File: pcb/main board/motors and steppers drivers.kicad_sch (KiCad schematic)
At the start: 35 parts, among them J1 Motor 0 Conn, J2 Motor 1 Conn, J3 Motor 2 Conn, J4 Motor 3 Conn, J7 Stepper 0 Conn, J8 Stepper 1 Conn, J9 Stepper 2 Conn, U1 L298HN, U2 L298HN

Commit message: Modified LM2596S to be a module.
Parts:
- C1, C2, C3, C4: footprint (none) -> Capacitor_THT:C_Disc_D6.0mm_W2.5mm_P5.00mm
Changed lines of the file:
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@@
 			)
 		)
-		(property "Footprint" ""
+		(property "Footprint" "Capacitor_THT:C_Disc_D6.0mm_W2.5mm_P5.00mm"
 			(at 73.66 35.2552 0)
 			(effects
@@
 			)
 		)
-		(property "Footprint" ""
+		(property "Footprint" "Capacitor_THT:C_Disc_D6.0mm_W2.5mm_P5.00mm"
 			(at 55.88 35.2552 0)
 			(effects
@@
 			)
 		)
-		(property "Footprint" ""
+		(property "Footprint" "Capacitor_THT:C_Disc_D6.0mm_W2.5mm_P5.00mm"
 			(at 213.36 33.3248 0)
 			(effects
@@
 			)
 		)
-		(property "Footprint" ""
+		(property "Footprint" "Capacitor_THT:C_Disc_D6.0mm_W2.5mm_P5.00mm"
 			(at 195.58 33.3248 0)
 			(effects

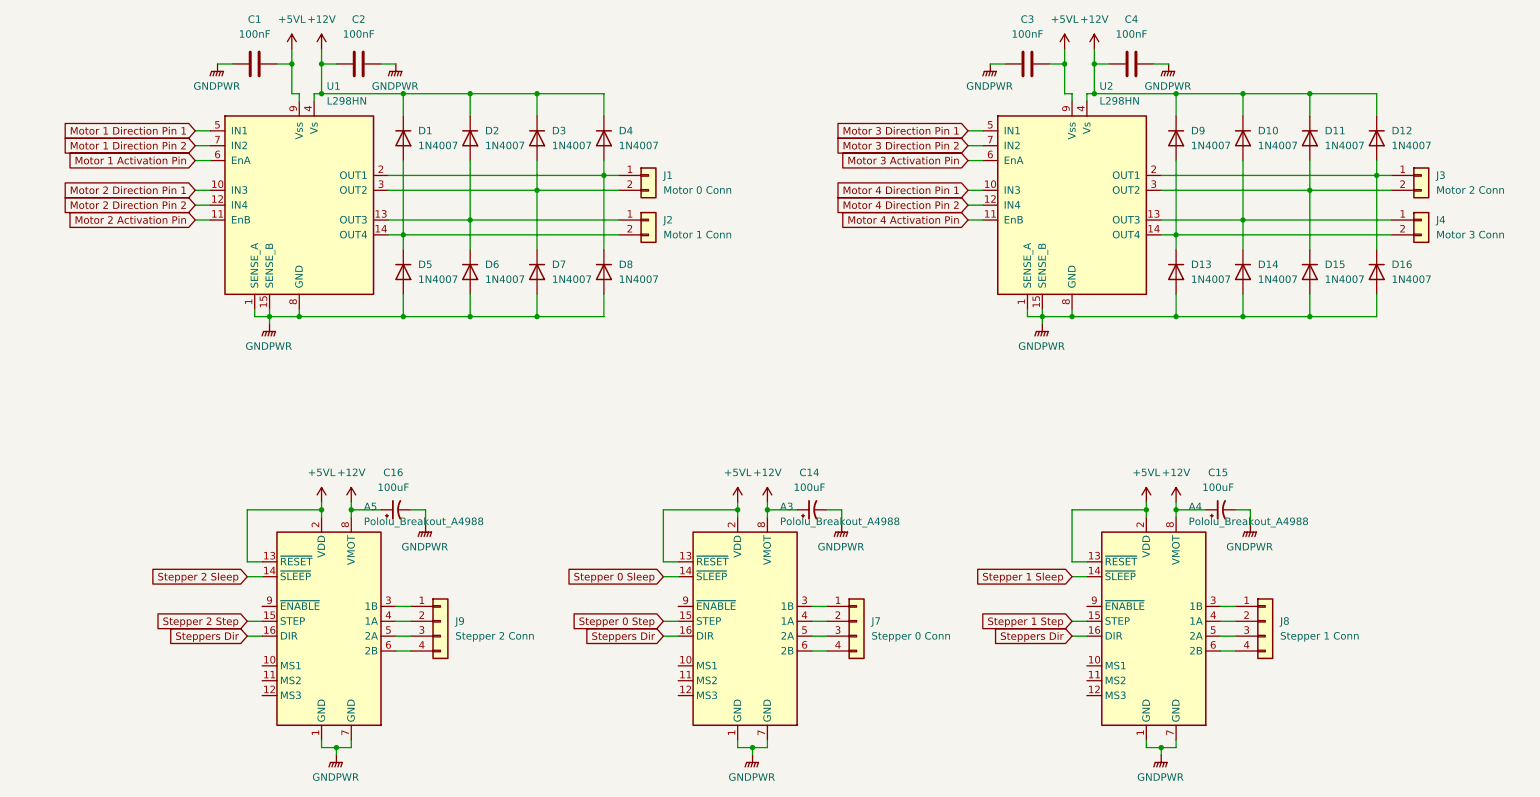
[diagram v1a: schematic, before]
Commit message: Changed some capacitors and assigned every component.
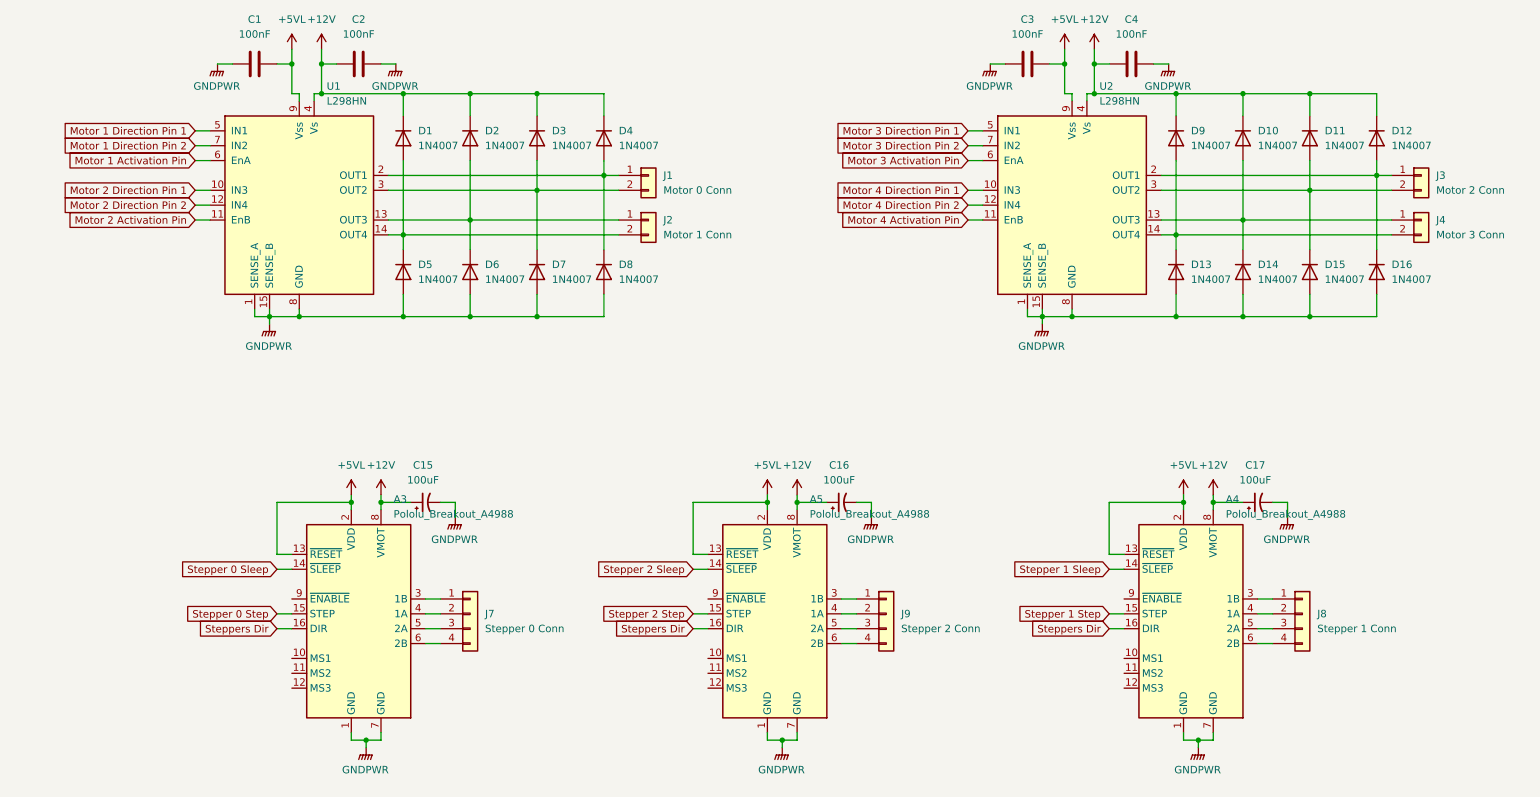
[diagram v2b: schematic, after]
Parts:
- C1, C2, C3, C4: footprint Capacitor_THT:C_Disc_D6.0mm_W2.5mm_P5.00mm -> Capacitor_THT:C_Disc_D4.3mm_W1.9mm_P5.00mm
- C15: renamed from C14; footprint (none) -> Capacitor_THT:CP_Radial_D10.0mm_P5.00mm
- C16: footprint (none) -> Capacitor_THT:CP_Radial_D10.0mm_P5.00mm
- C17: renamed from C15; footprint (none) -> Capacitor_THT:CP_Radial_D10.0mm_P5.00mm
- J1, J2, J3, J4: footprint (none) -> Connector:JWT_A3963_1x02_P3.96mm_Vertical
- J7, J8, J9: footprint (none) -> Connector:FanPinHeader_1x04_P2.54mm_Vertical
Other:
- moved on the sheet: A3, A4, A5, C15, C16, C17, J7, J8, J9

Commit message: Started Motors Wiring
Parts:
- J1, J2, J3, J4: footprint Connector:JWT_A3963_1x02_P3.96mm_Vertical -> Connector_PinHeader_2.54mm:PinHeader_1x02_P2.54mm_Vertical
- J7, J8, J9: footprint Connector:FanPinHeader_1x04_P2.54mm_Vertical -> Connector_PinHeader_2.54mm:PinHeader_1x04_P2.54mm_Vertical
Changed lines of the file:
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@@
 			)
 		)
-		(property "Footprint" "Connector:JWT_A3963_1x02_P3.96mm_Vertical"
+		(property "Footprint" "Connector_PinHeader_2.54mm:PinHeader_1x02_P2.54mm_Vertical"
 			(at 127 53.34 0)
 			(effects
@@
 			)
 		)
-		(property "Footprint" "Connector:JWT_A3963_1x02_P3.96mm_Vertical"
+		(property "Footprint" "Connector_PinHeader_2.54mm:PinHeader_1x02_P2.54mm_Vertical"
 			(at 259.08 53.34 0)
 			(effects
@@
 			)
 		)
-		(property "Footprint" "Connector:FanPinHeader_1x04_P2.54mm_Vertical"
+		(property "Footprint" "Connector_PinHeader_2.54mm:PinHeader_1x04_P2.54mm_Vertical"
 			(at 96.52 128.27 0)
 			(effects
@@
 			)
 		)
-		(property "Footprint" "Connector:FanPinHeader_1x04_P2.54mm_Vertical"
+		(property "Footprint" "Connector_PinHeader_2.54mm:PinHeader_1x04_P2.54mm_Vertical"
 			(at 238.76 128.27 0)
 			(effects
@@
 			)
 		)
-		(property "Footprint" "Connector:JWT_A3963_1x02_P3.96mm_Vertical"
+		(property "Footprint" "Connector_PinHeader_2.54mm:PinHeader_1x02_P2.54mm_Vertical"
 			(at 127 60.96 0)
 			(effects
@@
 			)
 		)
-		(property "Footprint" "Connector:JWT_A3963_1x02_P3.96mm_Vertical"
+		(property "Footprint" "Connector_PinHeader_2.54mm:PinHeader_1x02_P2.54mm_Vertical"
 			(at 259.08 60.96 0)
 			(effects
@@
 			)
 		)
-		(property "Footprint" "Connector:FanPinHeader_1x04_P2.54mm_Vertical"
+		(property "Footprint" "Connector_PinHeader_2.54mm:PinHeader_1x04_P2.54mm_Vertical"
 			(at 167.64 128.27 0)
 			(effects

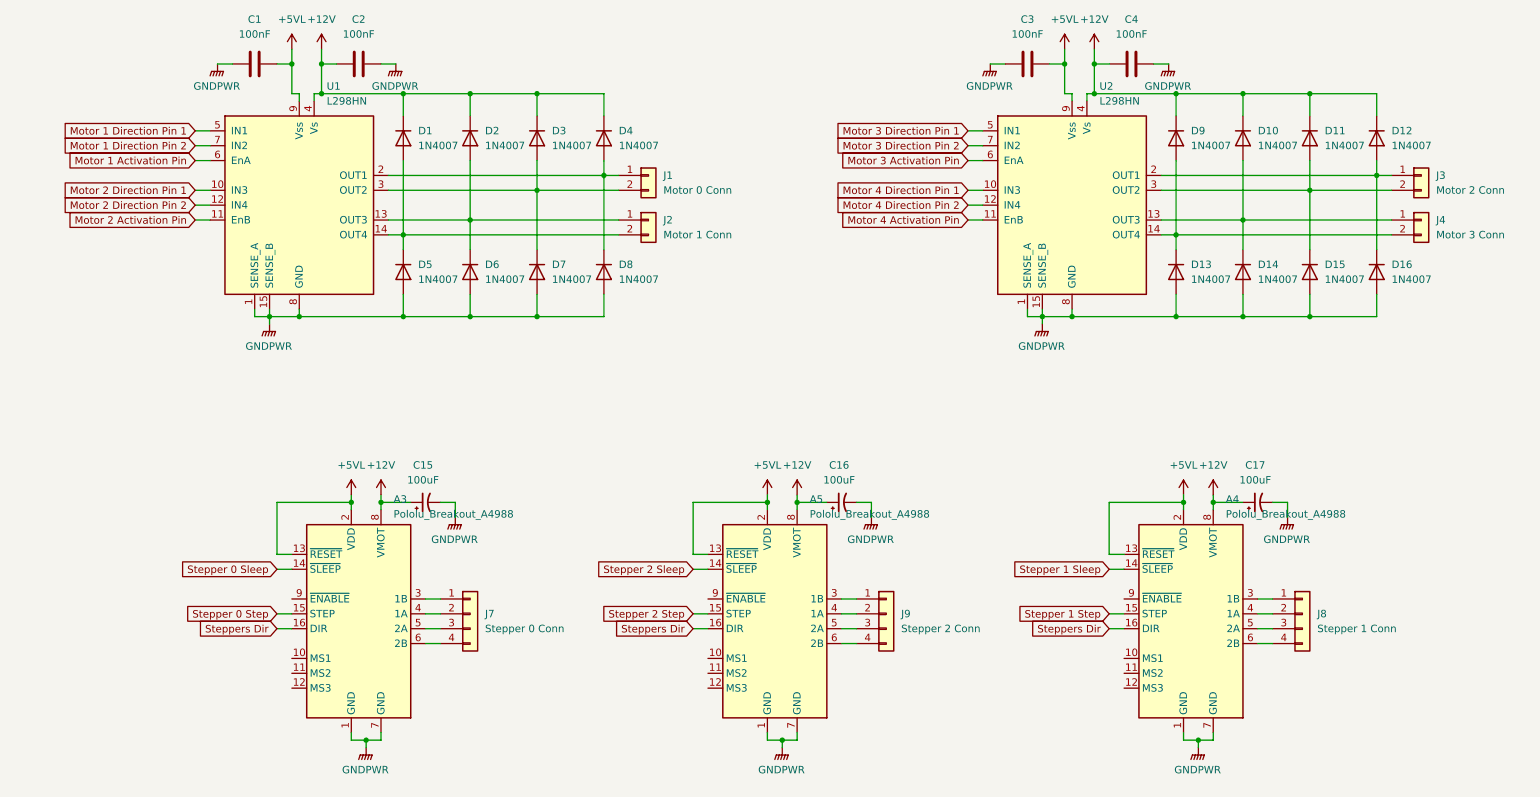
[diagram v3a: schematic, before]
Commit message: Finished DC motors wiring aand started 5VP regulator.
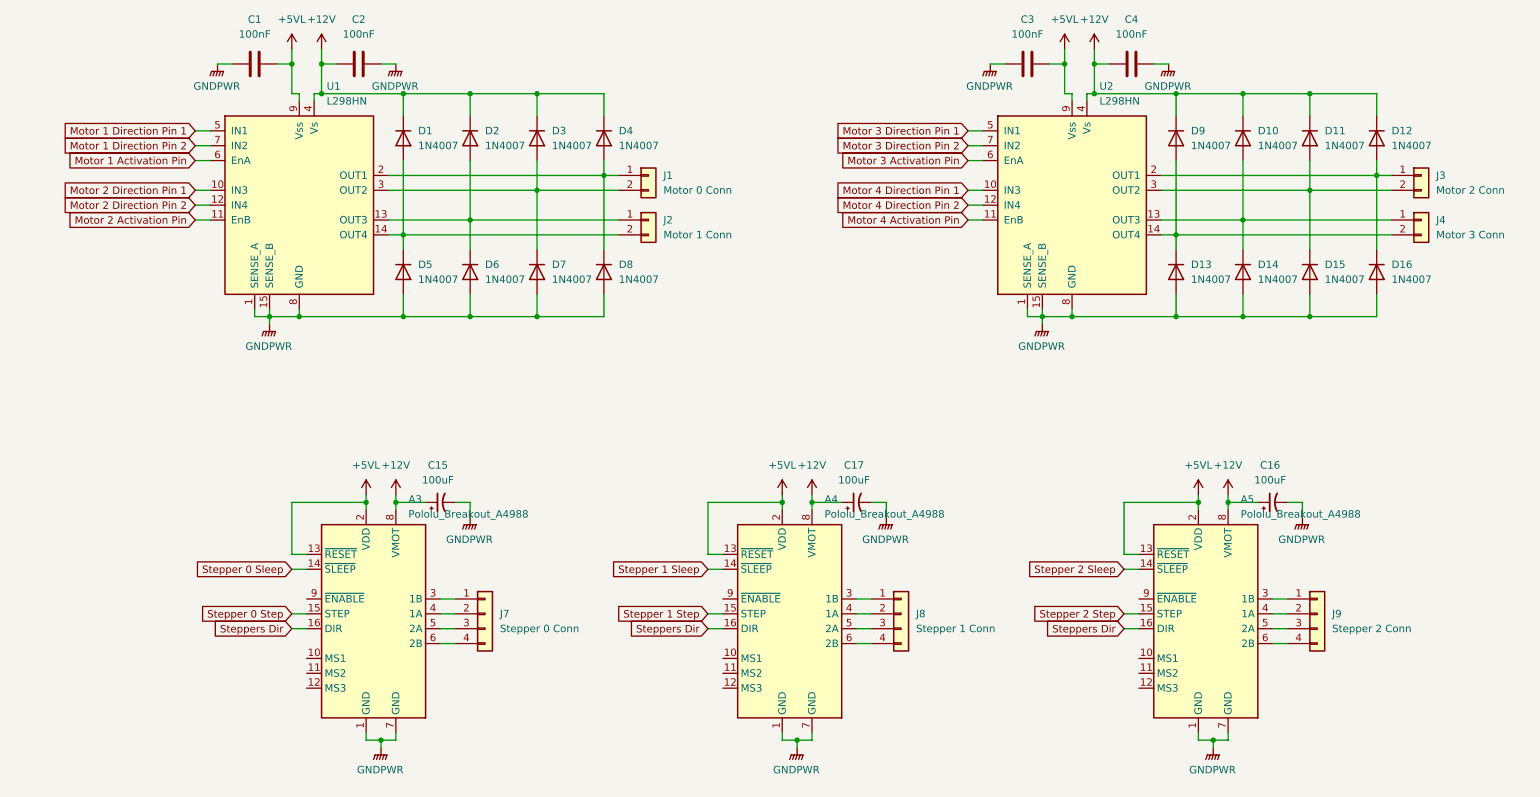
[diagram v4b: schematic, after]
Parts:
- C15, C16, C17: footprint Capacitor_THT:CP_Radial_D10.0mm_P5.00mm -> Capacitor_THT:CP_Radial_D5.0mm_P2.50mm
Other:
- moved on the sheet: A3, A4, A5, C15, C16, C17, J7, J8, J9

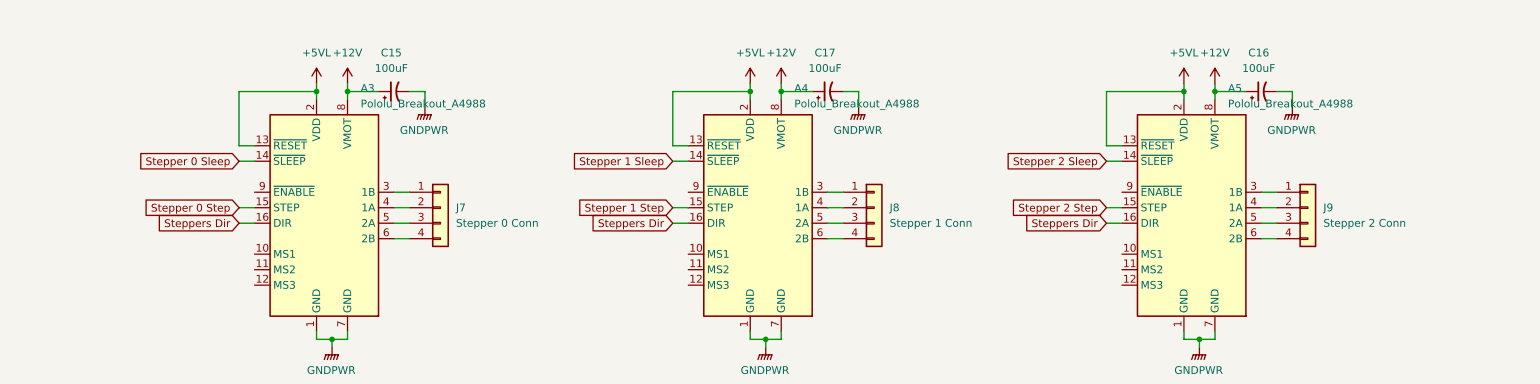
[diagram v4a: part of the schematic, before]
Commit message: Almost finished wiring motors drivers and continued connecting the rest. Also modified the LM2596S Module to put a hole in the board
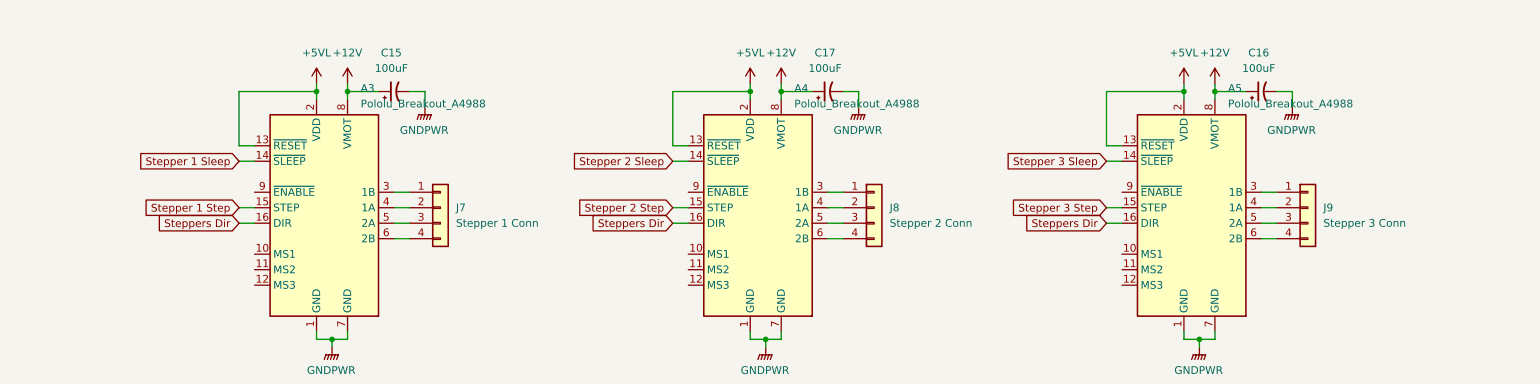
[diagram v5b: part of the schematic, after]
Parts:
- J7: value Stepper 0 Conn -> Stepper 1 Conn
- J8: value Stepper 1 Conn -> Stepper 2 Conn
- J9: value Stepper 2 Conn -> Stepper 3 Conn
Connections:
- net Stepper 0 Sleep is gone; now on net Stepper 1 Sleep: A3.14 (~{SLEEP})
- net Stepper 0 Step is gone; now on net Stepper 1 Step: A3.15 (STEP)
- net Stepper 1 Sleep: no longer A4.14 (~{SLEEP})
- net Stepper 1 Step: no longer A4.15 (STEP)
- net Stepper 2 Sleep: now also A4.14 (~{SLEEP}); no longer A5.14 (~{SLEEP})
- net Stepper 2 Step: now also A4.15 (STEP); no longer A5.15 (STEP)
- new net Stepper 3 Sleep: A5.14 (~{SLEEP})
- new net Stepper 3 Step: A5.15 (STEP)
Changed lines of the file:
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@@
 		)
 	)
-	(global_label "Stepper 0 Step"
+	(global_label "Stepper 1 Step"
 		(shape input)
 		(at 66.04 128.27 180)
@@
 		)
 	)
-	(global_label "Stepper 2 Step"
+	(global_label "Stepper 3 Step"
 		(shape input)
 		(at 208.28 128.27 180)
@@
 		)
 	)
-	(global_label "Stepper 1 Sleep"
+	(global_label "Stepper 2 Sleep"
 		(shape input)
 		(at 137.16 120.65 180)
@@
 		)
 	)
-	(global_label "Stepper 1 Step"
+	(global_label "Stepper 2 Step"
 		(shape input)
 		(at 137.16 128.27 180)
@@
 		)
 	)
-	(global_label "Stepper 0 Sleep"
+	(global_label "Stepper 1 Sleep"
 		(shape input)
 		(at 66.04 120.65 180)
@@
 		)
 	)
-	(global_label "Stepper 2 Sleep"
+	(global_label "Stepper 3 Sleep"
 		(shape input)
 		(at 208.28 120.65 180)
@@
 			)
 		)
-		(property "Value" "Stepper 0 Conn"
+		(property "Value" "Stepper 1 Conn"
 			(at 101.6 130.8099 0)
 			(effects
@@
 			)
 		)
-		(property "Value" "Stepper 1 Conn"
+		(property "Value" "Stepper 2 Conn"
 			(at 172.72 130.8099 0)
 			(effects
@@
 			)
 		)
-		(property "Value" "Stepper 2 Conn"
+		(property "Value" "Stepper 3 Conn"
 			(at 243.84 130.8099 0)
 			(effects

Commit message: Changed largeur of pistes and finished rewiring DC motors drivers
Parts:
- U1, U2: footprint Package_TO_SOT_THT:TO-220-15_P2.54x2.54mm_StaggerOdd_Lead5.84mm_TabDown -> Package_TO_SOT_THT:TO-220-15_P2.54x5.08mm_StaggerOdd_Lead4.58mm_Vertical
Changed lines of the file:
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@@
 			)
 		)
-		(property "Footprint" "Package_TO_SOT_THT:TO-220-15_P2.54x2.54mm_StaggerOdd_Lead5.84mm_TabDown"
+		(property "Footprint" "Package_TO_SOT_THT:TO-220-15_P2.54x5.08mm_StaggerOdd_Lead4.58mm_Vertical"
 			(at 68.58 74.93 0)
 			(effects
@@
 			)
 		)
-		(property "Footprint" "Package_TO_SOT_THT:TO-220-15_P2.54x2.54mm_StaggerOdd_Lead5.84mm_TabDown"
+		(property "Footprint" "Package_TO_SOT_THT:TO-220-15_P2.54x5.08mm_StaggerOdd_Lead4.58mm_Vertical"
 			(at 200.66 74.93 0)
 			(effects

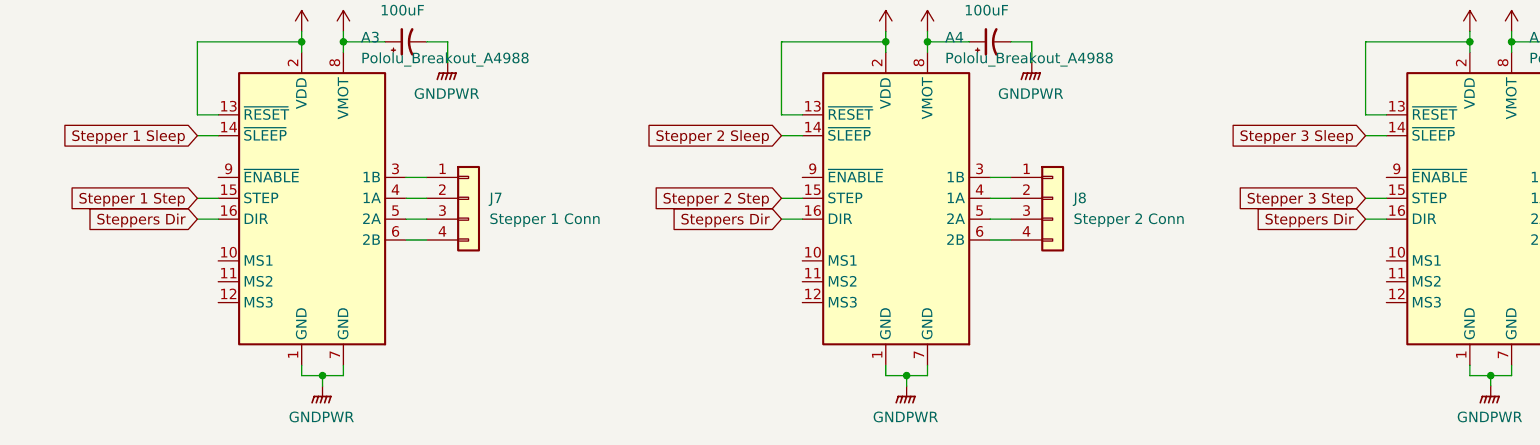
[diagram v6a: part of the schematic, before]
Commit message: Added Aisler DRC and corrected errors.
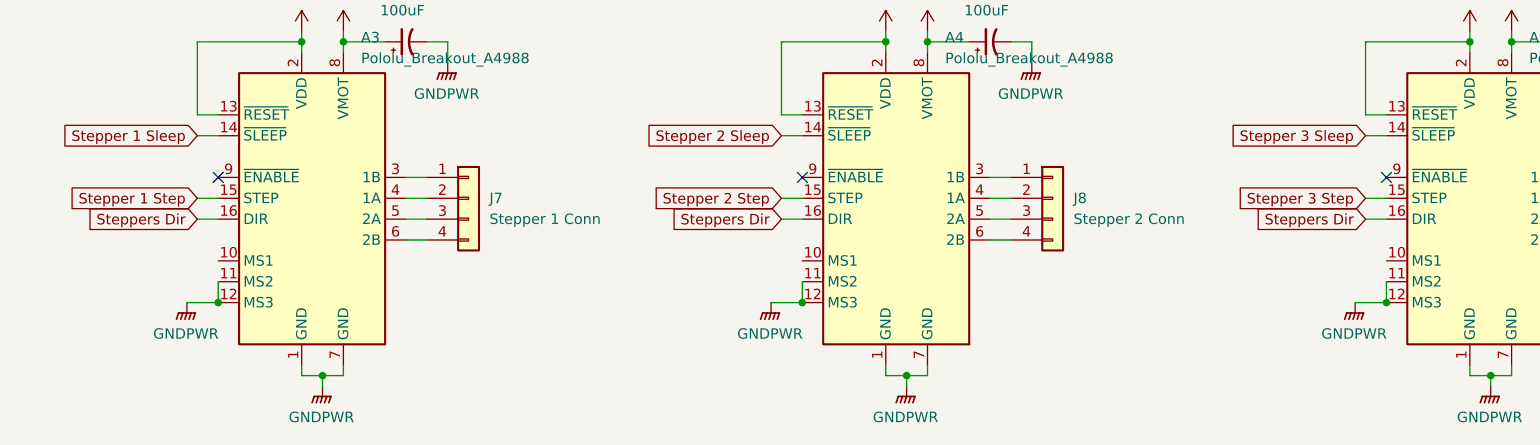
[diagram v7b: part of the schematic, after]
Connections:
- net GNDPWR: now also A3.11 (MS2), A3.12 (MS3), A4.11 (MS2), A4.12 (MS3), A5.11 (MS2), A5.12 (MS3)
- no-connect marks 0 -> 3

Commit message: Added motors encoders connectors
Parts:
- C15, C16, C17: footprint Capacitor_THT:CP_Radial_D5.0mm_P2.50mm -> Capacitor_THT:CP_Radial_D6.3mm_P2.50mm
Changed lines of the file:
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@@
 			)
 		)
-		(property "Footprint" "Capacitor_THT:CP_Radial_D5.0mm_P2.50mm"
+		(property "Footprint" "Capacitor_THT:CP_Radial_D6.3mm_P2.50mm"
 			(at 91.44 109.22 0)
 			(effects
@@
 			)
 		)
-		(property "Footprint" "Capacitor_THT:CP_Radial_D5.0mm_P2.50mm"
+		(property "Footprint" "Capacitor_THT:CP_Radial_D6.3mm_P2.50mm"
 			(at 162.56 109.22 0)
 			(effects
@@
 			)
 		)
-		(property "Footprint" "Capacitor_THT:CP_Radial_D5.0mm_P2.50mm"
+		(property "Footprint" "Capacitor_THT:CP_Radial_D6.3mm_P2.50mm"
 			(at 233.68 109.22 0)
 			(effects
